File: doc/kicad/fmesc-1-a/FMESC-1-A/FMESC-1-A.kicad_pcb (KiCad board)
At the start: 2 copper layers, 48 x 48 mm, 118 parts, among them Q1 AON6504, Q10 AON6504, Q11 AON6504, Q12 AON6504, Q13 AON6504, Q14 AON6504, Q15 AON6504, Q16 AON6504, Q17 AON6504, Q18 AON6504, Q19 AON6504, Q2 AON6504, Q20 AON6504, Q21 AON6504, Q22 AON6504, Q23 AON6504, Q24 AON6504, Q3 AON6504, Q4 AON6504, Q5 AON6504, Q6 AON6504, Q7 AON6504, Q8 AON6504, Q9 AON6504, U1 FD6288Q, U2 FD6288Q, U3 FD6288Q, U4 FD6288Q

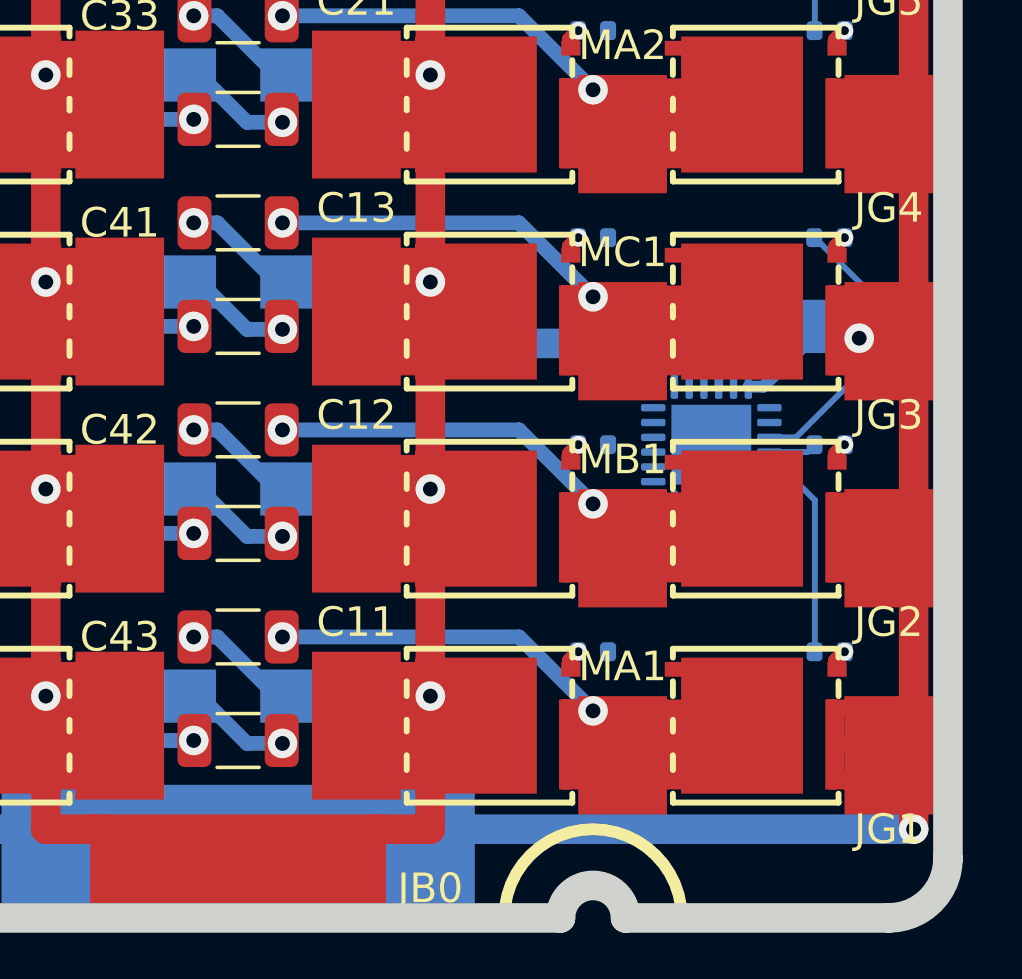
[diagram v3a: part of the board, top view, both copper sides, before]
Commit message: doc/kicad: FMESC-1-A  PCB wire fail
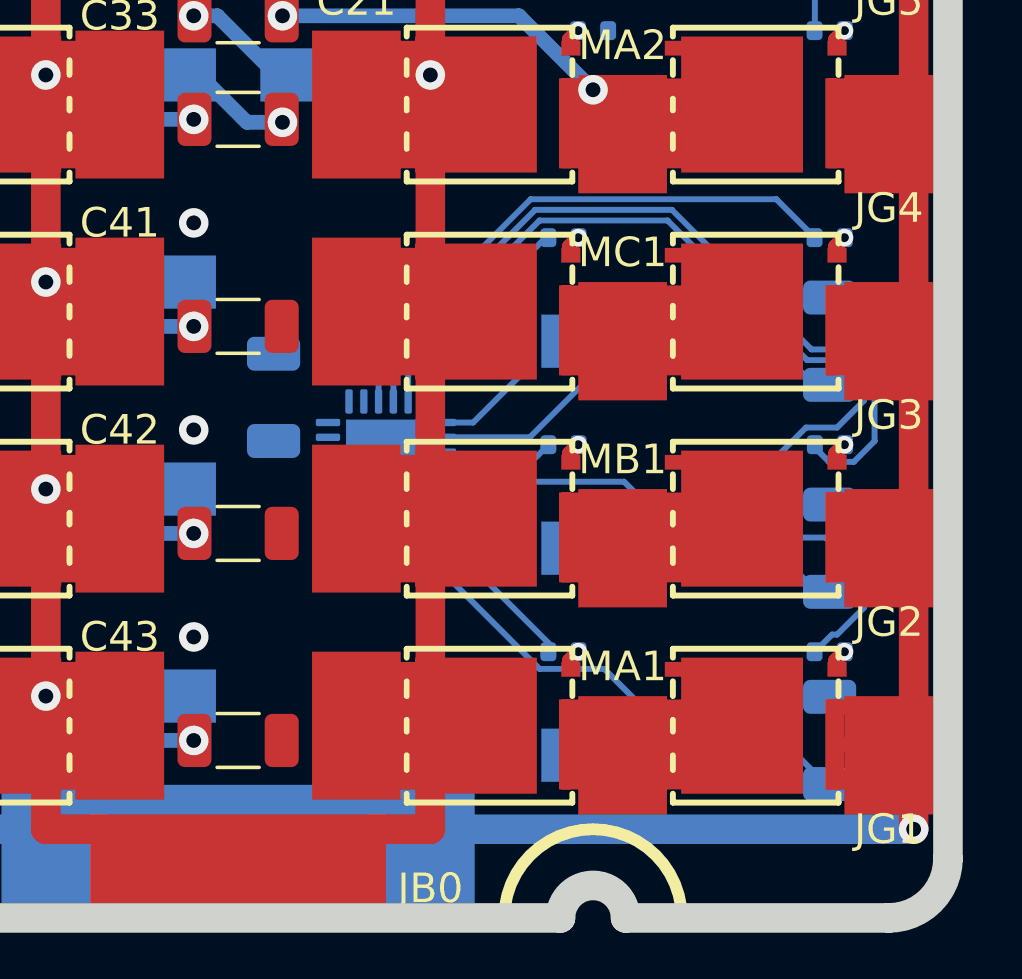
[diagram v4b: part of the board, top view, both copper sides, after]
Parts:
- C11, C12, C13: moved to B.Cu
- moved C12 20.4 mm to (94.0, 85.5), turned to 90 degrees
- moved C13 20.4 mm to (94.0, 78.5), turned to 90 degrees
- moved C11 20.3 mm to (94.0, 92.0), turned to 90 degrees
- moved C10 17.0 mm to (75.2, 80.4), turned to 270 degrees
- moved U1 11.0 mm to (79.0, 82.5), turned to 0 degrees
- moved D11 9.71 mm to (87.5, 92.5), turned to 180 degrees
- moved D12 9.71 mm to (87.5, 85.5), turned to 180 degrees
- moved D13 9.71 mm to (87.5, 78.5), turned to 180 degrees
- moved R12 1.00 mm to (85.0, 89.0), turned to 180 degrees
- moved R14 1.00 mm to (85.0, 82.0), turned to 180 degrees
- moved R16 1.00 mm to (85.0, 75.0), turned to 180 degrees
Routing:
- net /M1/ALG: track 7.13 -> 35.5 mm
- net /M1/BLG: track 1.64 -> 27.2 mm
- net Net-(C11-Pad1): track 3.20 -> 17.4 mm
- net +BATT: track 269.2 -> 256.5 mm, vias 12 -> 9
- net /M1/B1: track 24.5 -> 12.9 mm, vias 2 -> 0
- net /M1/C1: track 23.8 -> 12.2 mm, vias 2 -> 0
- net /M1/A1: track 24.6 -> 13.0 mm, vias 2 -> 0
- net Net-(C12-Pad1): track 3.20 -> 13.8 mm
- net Net-(C13-Pad1): track 3.63 -> 13.6 mm
- net /M1/CLG: track 9.79 -> 19.1 mm
- net /M1/CHG: track 0.00 -> 8.25 mm
- net /M1/AHG: track 0.00 -> 6.59 mm
- net GND: track 175.3 -> 171.0 mm, vias 6 -> 5
- net /M1/BHG: track 0.00 -> 3.85 mm
- net Net-(C43-Pad1): track 3.04 -> 0.00 mm, vias 1 -> 0
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
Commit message: doc/kicad: FMESC-1-A update PCB
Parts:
- removed C10, C11, C12, C13, C20, C21, C22, C23, C30, C31, C32, C33, C40, C41, C42, C43: 10u, Capacitor_SMD:C_1206_3216Metric
- removed D11, D12, D13, D21, D22, D23, D31, D32, D33, D41, D42, D43: D, Diode_SMD:D_SMA
- removed R11, R12, R13, R14, R15, R16, R21, R22, R23, R24, R25, R26, R31, R32, R33, R34, R35, R36, R41, R42, R43, R44, R45, R46: 10, Resistor_SMD:R_0402_1005Metric
- removed U1, U2, U3, U4: FD6288Q, Package_DFN_QFN:QFN-24-1EP_4x4mm_P0.5mm_EP2.7x2.7mm
- added J1: Conn_01x02, fmlibf:JS_2P_1.0mm, F.Cu at (86.5, 77.0)
- added J10: Conn_01x02, fmlibf:JS_2P_1.0mm, F.Cu at (86.5, 86.7)
- added J11: Conn_01x02, fmlibf:JS_2P_1.0mm, F.Cu at (80.2, 88.9)
- added J12: Conn_01x02, fmlibf:JS_2P_1.0mm, F.Cu at (86.5, 84.5)
- added J13: Conn_01x02, fmlibf:JS_2P_1.0mm, F.Cu at (105.4, 77.0)
- added J14: Conn_01x02, fmlibf:JS_2P_1.0mm, F.Cu at (99.1, 79.2)
- added J15: Conn_01x02, fmlibf:JS_2P_1.0mm, F.Cu at (99.1, 74.8)
- added J16: Conn_01x02, fmlibf:JS_2P_1.0mm, F.Cu at (105.4, 74.8)
- added J17: Conn_01x02, fmlibf:JS_2P_1.0mm, F.Cu at (99.1, 77.0)
- added J18: Conn_01x02, fmlibf:JS_2P_1.0mm, F.Cu at (105.4, 72.6)
- added J19: Conn_01x02, fmlibf:JS_2P_1.0mm, F.Cu at (99.1, 84.5)
- added J2: Conn_01x02, fmlibf:JS_2P_1.0mm, F.Cu at (80.2, 72.6)
- added J20: Conn_01x02, fmlibf:JS_2P_1.0mm, F.Cu at (99.1, 86.7)
- added J21: Conn_01x02, fmlibf:JS_2P_1.0mm, F.Cu at (105.4, 84.5)
- added J22: Conn_01x02, fmlibf:JS_2P_1.0mm, F.Cu at (99.1, 88.9)
- added J23: Conn_01x02, fmlibf:JS_2P_1.0mm, F.Cu at (105.4, 86.7)
- added J24: Conn_01x02, fmlibf:JS_2P_1.0mm, F.Cu at (99.1, 91.1)
- added J3: Conn_01x02, fmlibf:JS_2P_1.0mm, F.Cu at (80.2, 74.8)
- added J4: Conn_01x02, fmlibf:JS_2P_1.0mm, F.Cu at (86.5, 72.6)
- added J5: Conn_01x02, fmlibf:JS_2P_1.0mm, F.Cu at (80.2, 77.0)
- added J6: Conn_01x02, fmlibf:JS_2P_1.0mm, F.Cu at (86.5, 74.8)
- added J7: Conn_01x02, fmlibf:JS_2P_1.0mm, F.Cu at (86.5, 88.9)
- added J8: Conn_01x02, fmlibf:JS_2P_1.0mm, F.Cu at (80.2, 91.1)
- added J9: Conn_01x02, fmlibf:JS_2P_1.0mm, F.Cu at (80.2, 84.5)
- added JP1: Conn_01x02, fmlibf:JS_2P_1.0mm, F.Cu at (80.2, 79.2)
- added JP2: Conn_01x02, fmlibf:JS_2P_1.0mm, F.Cu at (80.2, 86.7)
- added JP3: Conn_01x02, fmlibf:JS_2P_1.0mm, F.Cu at (99.1, 72.6)
- added JP4: Conn_01x02, fmlibf:JS_2P_1.0mm, F.Cu at (105.4, 88.9)
- JG1, JG10, JG11, JG12, JG2, JG3, JG4, JG5, JG6, JG7, JG8, JG9, MA1, MA2, MA3, MA4, MB1, MB2, MB3, MB4, MC1, MC2, MC3, MC4: footprint fmlibf:JS3x4mm -> fmlibf:JS3x3.5mm
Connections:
- Q1 pad 2: Net-(Q1-Pad2) -> /M1/ALG
- Q10 pad 2: Net-(Q10-Pad2) -> /M2/BHG
- Q11 pad 2: Net-(Q11-Pad2) -> /M2/CLG
- Q12 pad 2: Net-(Q12-Pad2) -> /M2/CHG
- Q13 pad 2: Net-(Q13-Pad2) -> /M3/ALG
- Q14 pad 2: Net-(Q14-Pad2) -> /M3/AHG
- Q15 pad 2: Net-(Q15-Pad2) -> /M3/BLG
- Q16 pad 2: Net-(Q16-Pad2) -> /M3/BHG
- Q17 pad 2: Net-(Q17-Pad2) -> /M3/CLG
- Q18 pad 2: Net-(Q18-Pad2) -> /M3/CHG
- Q19 pad 2: Net-(Q19-Pad2) -> /M4/ALG
- Q2 pad 2: Net-(Q2-Pad2) -> /M1/AHG
- Q20 pad 2: Net-(Q20-Pad2) -> /M4/AHG
- Q21 pad 2: Net-(Q21-Pad2) -> /M4/BLG
- Q22 pad 2: Net-(Q22-Pad2) -> /M4/BHG
- Q23 pad 2: Net-(Q23-Pad2) -> /M4/CLG
- Q24 pad 2: Net-(Q24-Pad2) -> /M4/CHG
- Q3 pad 2: Net-(Q3-Pad2) -> /M1/BLG
- Q4 pad 2: Net-(Q4-Pad2) -> /M1/BHG
- Q5 pad 2: Net-(Q5-Pad2) -> /M1/CLG
- Q6 pad 2: Net-(Q6-Pad2) -> /M1/CHG
- Q7 pad 2: Net-(Q7-Pad2) -> /M2/ALG
- Q8 pad 2: Net-(Q8-Pad2) -> /M2/AHG
- Q9 pad 2: Net-(Q9-Pad2) -> /M2/BLG
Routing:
- net /M1/ALG: track 35.5 -> 36.2 mm, vias 0 -> 1
- net Net-(Q9-Pad2): track 0.62 -> 0.00 mm, vias 1 -> 0
- net Net-(Q8-Pad2): track 0.62 -> 0.00 mm, vias 1 -> 0
- net Net-(Q7-Pad2): track 0.62 -> 0.00 mm, vias 1 -> 0
- net Net-(Q6-Pad2): track 0.62 -> 0.00 mm, vias 1 -> 0
- net Net-(Q5-Pad2): track 0.62 -> 0.00 mm, vias 1 -> 0
- net Net-(Q4-Pad2): track 0.62 -> 0.00 mm, vias 1 -> 0
- net Net-(Q3-Pad2): track 0.62 -> 0.00 mm, vias 1 -> 0
- net Net-(Q24-Pad2): track 0.62 -> 0.00 mm, vias 1 -> 0
- net Net-(Q23-Pad2): track 0.62 -> 0.00 mm, vias 1 -> 0
- net Net-(Q22-Pad2): track 0.62 -> 0.00 mm, vias 1 -> 0
- net Net-(Q21-Pad2): track 0.62 -> 0.00 mm, vias 1 -> 0
- net Net-(Q20-Pad2): track 0.62 -> 0.00 mm, vias 1 -> 0
- net Net-(Q2-Pad2): track 0.62 -> 0.00 mm, vias 1 -> 0
- net Net-(Q19-Pad2): track 0.62 -> 0.00 mm, vias 1 -> 0
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
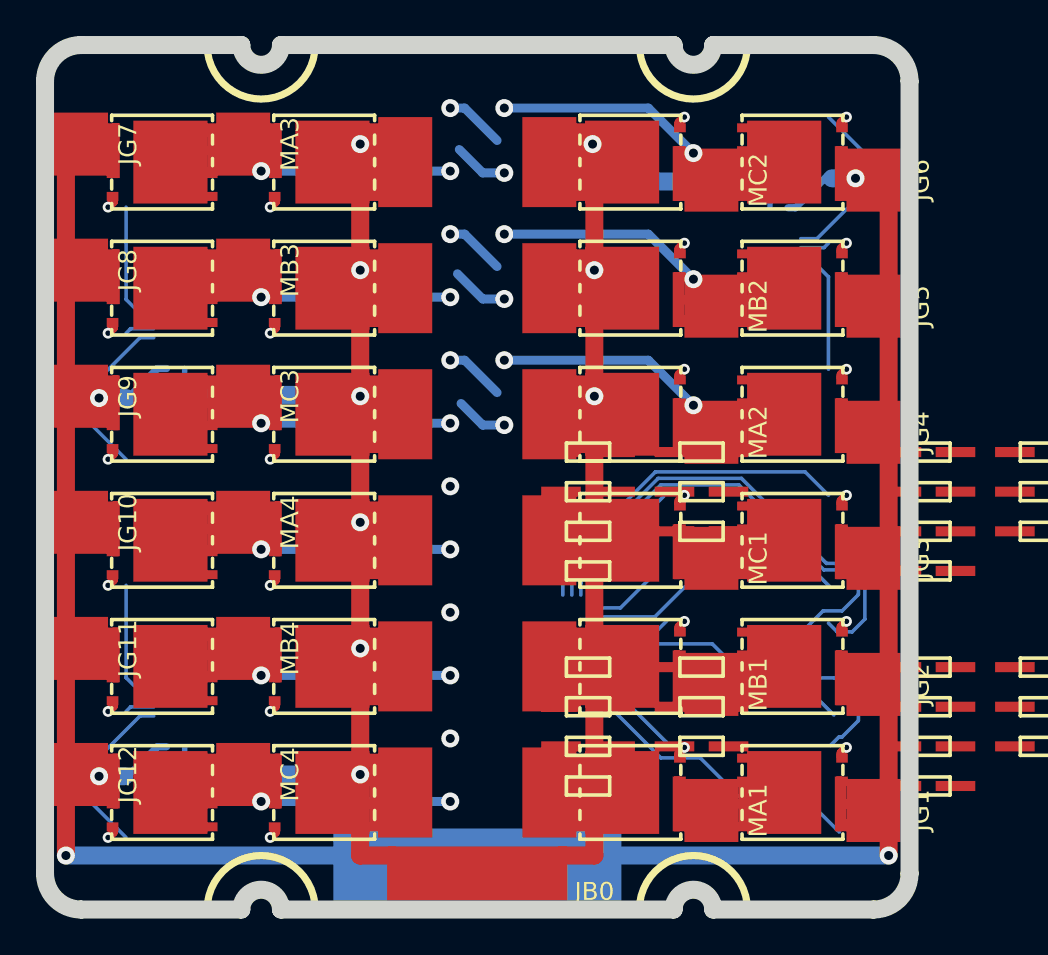
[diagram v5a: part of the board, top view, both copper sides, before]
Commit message: doc/kicad: FMESC-1-A clean PCB
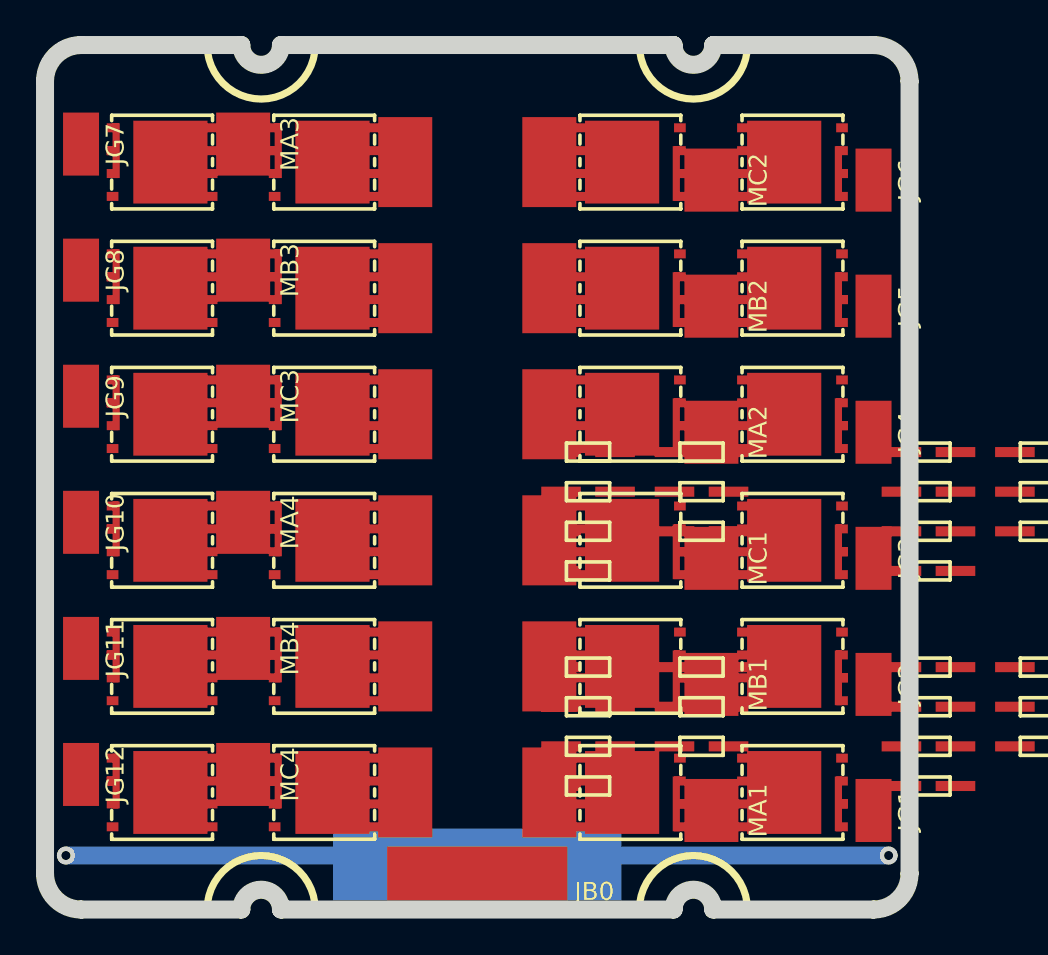
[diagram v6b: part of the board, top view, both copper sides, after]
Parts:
- JG1, JG10, JG11, JG12, JG2, JG3, JG4, JG5, JG6, JG7, JG8, JG9: footprint fmlibf:JS3x3.5mm -> fmlibf:JS2x3.5mm
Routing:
- net +BATT: track 256.5 -> 0.00 mm, vias 9 -> 0
- net GND: track 171.0 -> 31.7 mm, vias 5 -> 2
- net /M1/ALG: track 36.2 -> 0.00 mm, vias 1 -> 0
- net /M1/BLG: track 27.8 -> 0.00 mm, vias 1 -> 0
- net /M2/C1: track 23.8 -> 0.00 mm, vias 2 -> 0
- net /M2/A1: track 23.8 -> 0.00 mm, vias 2 -> 0
- net /M2/B1: track 23.5 -> 0.00 mm, vias 2 -> 0
- net /M4/B1: track 23.3 -> 0.00 mm, vias 2 -> 0
- net /M3/C1: track 23.2 -> 0.00 mm, vias 2 -> 0
- net /M4/C1: track 23.1 -> 0.00 mm, vias 2 -> 0
- net /M4/A1: track 23.0 -> 0.00 mm, vias 2 -> 0
- net /M3/B1: track 23.0 -> 0.00 mm, vias 2 -> 0
- net /M3/A1: track 23.0 -> 0.00 mm, vias 2 -> 0
- net /M1/CLG: track 19.7 -> 0.00 mm, vias 1 -> 0
- net Net-(C11-Pad1): track 17.4 -> 0.00 mm, vias 1 -> 0
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
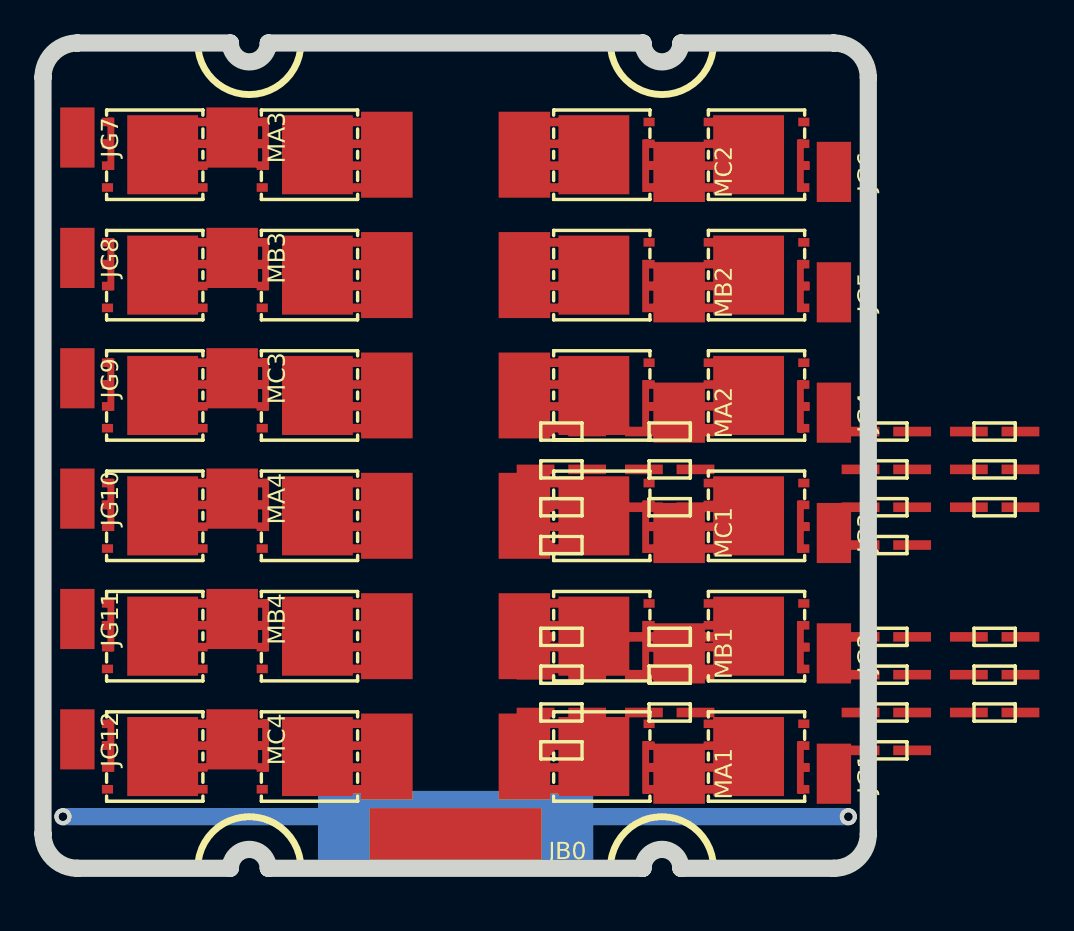
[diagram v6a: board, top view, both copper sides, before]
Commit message: doc/kicad: FMESC-1-A PCB layout
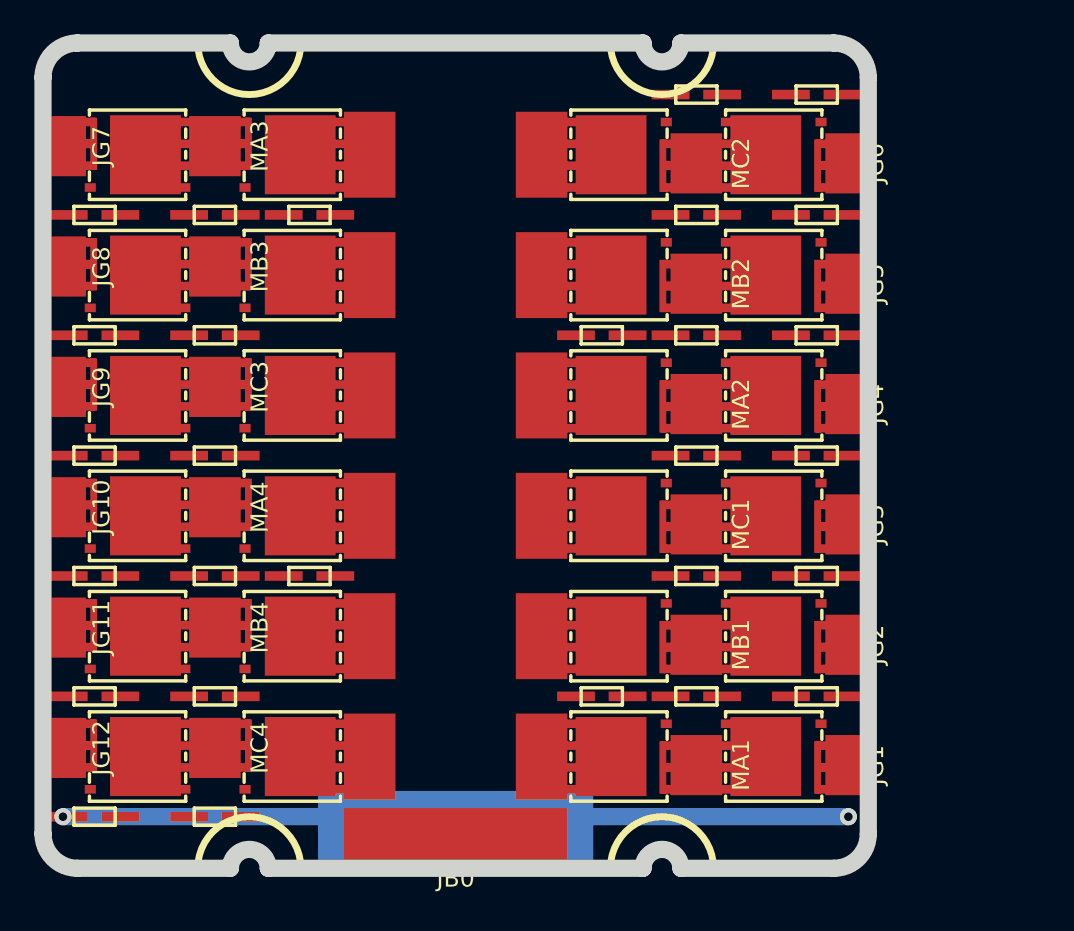
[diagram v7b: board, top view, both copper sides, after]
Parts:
- JB0: footprint fmlibf:JS3x10mm -> fmlibf:JS3x13mm
- moved J13 55.0 mm to (53.0, 60.0)
- moved J23 53.0 mm to (53.0, 95.0)
- moved J21 52.5 mm to (53.0, 88.0)
- moved J15 46.7 mm to (53.0, 67.0)
- moved J19 46.2 mm to (53.0, 81.0)
- moved J17 46.1 mm to (53.0, 74.0)
- moved J16 46.0 mm to (60.0, 67.0)
- moved J18 45.4 mm to (60.0, 74.0)
- moved J14 43.5 mm to (60.0, 60.0)
- moved JP4 40.6 mm to (65.5, 81.0)
- moved J20 39.5 mm to (60.0, 81.0)
- moved J24 39.2 mm to (60.0, 95.0)
- moved J22 39.1 mm to (60.0, 88.0)
- moved J11 38.9 mm to (95.0, 53.0), turned to 180 degrees
- moved JP3 35.8 mm to (65.5, 60.0)
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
